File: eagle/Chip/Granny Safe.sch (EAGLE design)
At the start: 86 parts, among them IC1 MCP604SL, J1 3x4 Keypad, J10 SCREW-4, J2 FEMALE 2x3, J3 SCREW-4, J4 i2c_16x2, J6 FEMALE 2x3, J8 RES JUMPER, Q1 TRANS_NPN-MMBTA42, Q2 TRANS_NPN-MMBTA42, Q3 TRANS_NPN-MMBTA42, Q4 2N3904, T1 BT137, U1 328P, U2 SFH6206, U3 MOC3051

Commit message: worked on board, should be all done
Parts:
- R17: value 5k -> 5.1k
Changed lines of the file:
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@@
 <part name="GND5" library="SparkFun-PowerSymbols" deviceset="GND" device=""/>
 <part name="VR1" library="SparkFun-Resistors" library_urn="urn:adsk.eagle:library:532" deviceset="TRIMPOT" device="-SMD-3MM-CLOSED-1/8W-20%" package3d_urn="urn:adsk.eagle:package:39665/1" value="10k"/>
-<part name="R17" library="resistor" library_urn="urn:adsk.eagle:library:348" deviceset="R-US_" device="R0603" package3d_urn="urn:adsk.eagle:package:26057/1" value="5k"/>
+<part name="R17" library="resistor" library_urn="urn:adsk.eagle:library:348" deviceset="R-US_" device="R0603" package3d_urn="urn:adsk.eagle:package:26057/1" value="5.1k"/>
 <part name="J6" library="SparkFun-Connectors" library_urn="urn:adsk.eagle:library:513" deviceset="CONN_03X2" device="FEMALE" package3d_urn="urn:adsk.eagle:package:38016/1" value="FEMALE 2x3"/>
 <part name="GND6" library="SparkFun-PowerSymbols" deviceset="GND" device=""/>

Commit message: update
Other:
- note added: "ADC TP"
- note added: "ALR JMP"
- note added: "GND TP"
- note added: "MCP6004"
- note added: "ON JMP"
- note added: "PWR JMP"
- note added: "RTD JMP"
- note added: "S1"
- note added: "SET JMP"
- note added: "SUP JMP"
- note added: "TIM JMP"
- note added: "ZERO TP"
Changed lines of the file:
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@@
 <text x="266.7" y="7.366" size="2.54" layer="94">C</text>
 <text x="199.898" y="166.624" size="1.778" layer="96">LM2576</text>
+<text x="38.354" y="29.21" size="1.778" layer="96">SET JMP</text>
+<text x="73.914" y="29.21" size="1.778" layer="96">TIM JMP</text>
+<text x="119.38" y="33.274" size="1.778" layer="96">ALR JMP</text>
+<text x="195.072" y="57.912" size="1.778" layer="96">GND TP</text>
+<text x="195.072" y="52.578" size="1.778" layer="96">GND TP</text>
+<text x="234.95" y="59.69" size="1.778" layer="96">ON JMP</text>
+<text x="257.048" y="134.366" size="1.778" layer="96">PWR JMP</text>
+<text x="160.782" y="186.69" size="1.778" layer="96">S1</text>
+<text x="108.458" y="192.024" size="1.778" layer="96">ADC TP</text>
+<text x="135.636" y="118.872" size="1.778" layer="96">ZERO TP</text>
+<text x="166.116" y="47.244" size="1.778" layer="96">SUP JMP</text>
+<text x="30.226" y="154.686" size="1.778" layer="96">RTD JMP</text>
+<text x="56.896" y="188.976" size="1.778" layer="96">MCP6004</text>
 </plain>
 <instances>
@@
 </instance>
 <instance part="T1" gate="G$1" x="221.488" y="93.98"/>
-<instance part="U3" gate="G$1" x="196.088" y="93.98" smashed="yes" rot="MR0">
-<attribute name="NAME" x="203.708" y="99.314" size="1.778" layer="95" font="vector" rot="MR0"/>
+<instance part="U3" gate="G$1" x="196.088" y="93.98" smashed="yes">
+<attribute name="NAME" x="188.468" y="99.314" size="1.778" layer="95" font="vector"/>
 </instance>
 <instance part="R26" gate="G$1" x="165.608" y="174.244" smashed="yes" rot="MR90">
@@
 </segment>
 </net>
-<net name="N$34" class="0">
-<segment>
-<pinref part="Q4" gate="G$1" pin="C"/>
-<wire x1="185.928" y1="91.44" x2="183.388" y2="91.44" width="0.1524" layer="91"/>
-<pinref part="U3" gate="G$1" pin="2"/>
-</segment>
-</net>
 <net name="PWR" class="0">
 <segment>
@@
 <pinref part="T1" gate="G$1" pin="A2"/>
 <wire x1="206.248" y1="99.06" x2="221.488" y2="99.06" width="0.1524" layer="91"/>
-<wire x1="206.248" y1="99.06" x2="206.248" y2="96.52" width="0.1524" layer="91"/>
-<pinref part="U3" gate="G$1" pin="6"/>
 <wire x1="221.488" y1="99.06" x2="232.918" y2="99.06" width="0.1524" layer="91"/>
 <junction x="221.488" y="99.06"/>
@@
 <junction x="232.918" y="122.428"/>
 <label x="250.698" y="122.428" size="1.778" layer="95"/>
+<pinref part="U3" gate="G$1" pin="6"/>
+<wire x1="206.248" y1="96.52" x2="206.248" y2="99.06" width="0.1524" layer="91"/>
 </segment>
 </net>
@@
 <wire x1="216.408" y1="93.98" x2="216.408" y2="91.44" width="0.1524" layer="91"/>
 <pinref part="T1" gate="G$1" pin="G"/>
-</segment>
-</net>
-<net name="N$31" class="0">
-<segment>
-<pinref part="R22" gate="G$1" pin="2"/>
-<pinref part="U3" gate="G$1" pin="1"/>
-</segment>
-</net>
-<net name="N$32" class="0">
-<segment>
-<pinref part="R24" gate="G$1" pin="1"/>
-<pinref part="U3" gate="G$1" pin="4"/>
 </segment>
 </net>
@@
 </segment>
 </net>
+<net name="N$31" class="0">
+<segment>
+<pinref part="U3" gate="G$1" pin="4"/>
+<pinref part="R24" gate="G$1" pin="1"/>
+</segment>
+</net>
+<net name="N$32" class="0">
+<segment>
+<pinref part="U3" gate="G$1" pin="1"/>
+<pinref part="R22" gate="G$1" pin="2"/>
+</segment>
+</net>
+<net name="N$34" class="0">
+<segment>
+<pinref part="Q4" gate="G$1" pin="C"/>
+<pinref part="U3" gate="G$1" pin="2"/>
+<wire x1="183.388" y1="91.44" x2="185.928" y2="91.44" width="0.1524" layer="91"/>
+</segment>
+</net>

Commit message: new stuff
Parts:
- removed R16: 1M, resistor:R-US_R0603
- removed VR2: 10k, SparkFun-Resistors:TRIMPOT-SMD-3MM-OPEN-1/10W-25%
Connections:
- new net N$42: D4.C
- net GND: now also D4.A, RTD.2; no longer D4.C, R16.1, VR2.CCW
- net N$13: now also RTD.1
- net N$33: no longer VR2.WIPER
- net N$38: no longer VR2.CW
- net N$41: no longer D4.A
- net ZERO: no longer R16.2
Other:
- moved on the sheet: D4, R26, R27, RTD

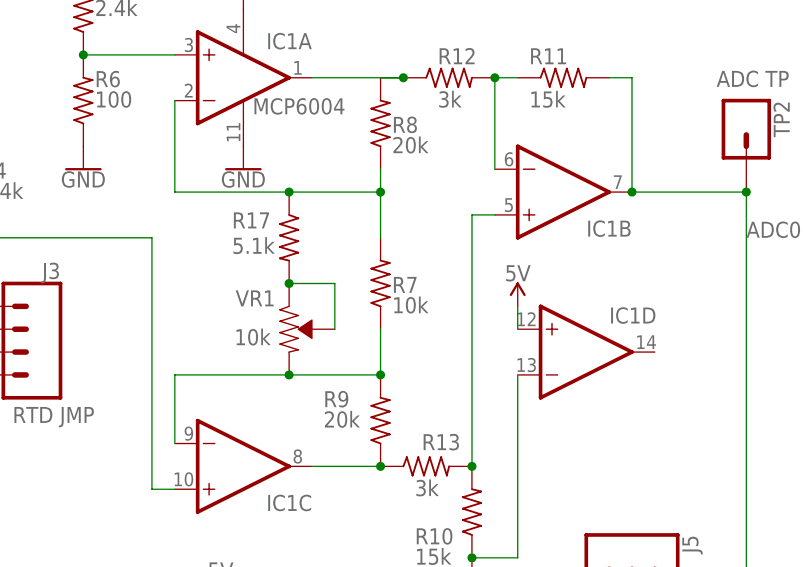
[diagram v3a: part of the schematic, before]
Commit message: but pres/report stuff in report folder
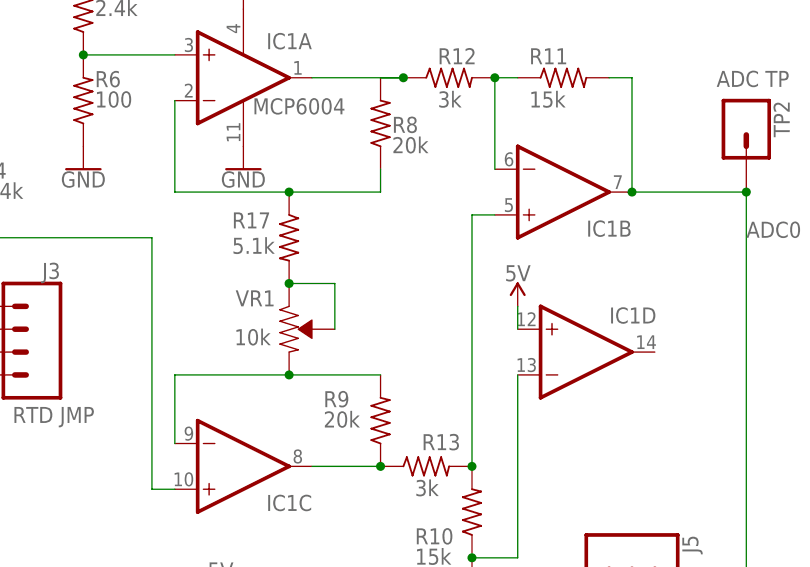
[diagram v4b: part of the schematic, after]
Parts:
- removed R7: 10k, resistor:R-US_R0603
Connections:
- net N$24: no longer R7.2
- net N$26: no longer R7.1
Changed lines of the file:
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@@
 <part name="R5" library="resistor" library_urn="urn:adsk.eagle:library:348" deviceset="R-US_" device="R0603" package3d_urn="urn:adsk.eagle:package:26057/1" value="2.4k"/>
 <part name="R6" library="resistor" library_urn="urn:adsk.eagle:library:348" deviceset="R-US_" device="R0603" package3d_urn="urn:adsk.eagle:package:26057/1" value="100"/>
-<part name="R7" library="resistor" library_urn="urn:adsk.eagle:library:348" deviceset="R-US_" device="R0603" package3d_urn="urn:adsk.eagle:package:26057/1" value="10k"/>
 <part name="R8" library="resistor" library_urn="urn:adsk.eagle:library:348" deviceset="R-US_" device="R0603" package3d_urn="urn:adsk.eagle:package:26057/1" value="20k"/>
 <part name="R9" library="resistor" library_urn="urn:adsk.eagle:library:348" deviceset="R-US_" device="R0603" package3d_urn="urn:adsk.eagle:package:26057/1" value="20k"/>
@@
 <attribute name="VALUE" x="39.37" y="189.738" size="1.778" layer="96"/>
 </instance>
-<instance part="R7" gate="G$1" x="71.12" y="170.18" smashed="yes" rot="R90">
-<attribute name="NAME" x="72.39" y="169.1386" size="1.778" layer="95"/>
-<attribute name="VALUE" x="72.39" y="166.878" size="1.778" layer="96"/>
-</instance>
 <instance part="R8" gate="G$1" x="71.12" y="187.96" smashed="yes" rot="R90">
 <attribute name="NAME" x="72.39" y="186.9186" size="1.778" layer="95"/>
@@
 <wire x1="60.96" y1="180.34" x2="71.12" y2="180.34" width="0.1524" layer="91"/>
 <wire x1="71.12" y1="180.34" x2="71.12" y2="182.88" width="0.1524" layer="91"/>
-<pinref part="R7" gate="G$1" pin="2"/>
-<wire x1="71.12" y1="180.34" x2="71.12" y2="175.26" width="0.1524" layer="91"/>
-<junction x="71.12" y="180.34"/>
 <pinref part="R17" gate="G$1" pin="1"/>
 <junction x="60.96" y="180.34"/>
@@
 <segment>
 <pinref part="R9" gate="G$1" pin="2"/>
-<pinref part="R7" gate="G$1" pin="1"/>
-<wire x1="71.12" y1="160.02" x2="71.12" y2="165.1" width="0.1524" layer="91"/>
 <pinref part="IC1" gate="C" pin="-IN"/>
 <wire x1="48.26" y1="152.4" x2="48.26" y2="160.02" width="0.1524" layer="91"/>
 <wire x1="48.26" y1="160.02" x2="60.96" y2="160.02" width="0.1524" layer="91"/>
-<junction x="71.12" y="160.02"/>
 <pinref part="VR1" gate="R?" pin="CCW"/>
 <wire x1="60.96" y1="160.02" x2="71.12" y2="160.02" width="0.1524" layer="91"/>
